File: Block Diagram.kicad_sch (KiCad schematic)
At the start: 0 parts

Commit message: Finished preliminary project schematics and architecture
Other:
- note added: "VBAT/VBUS"

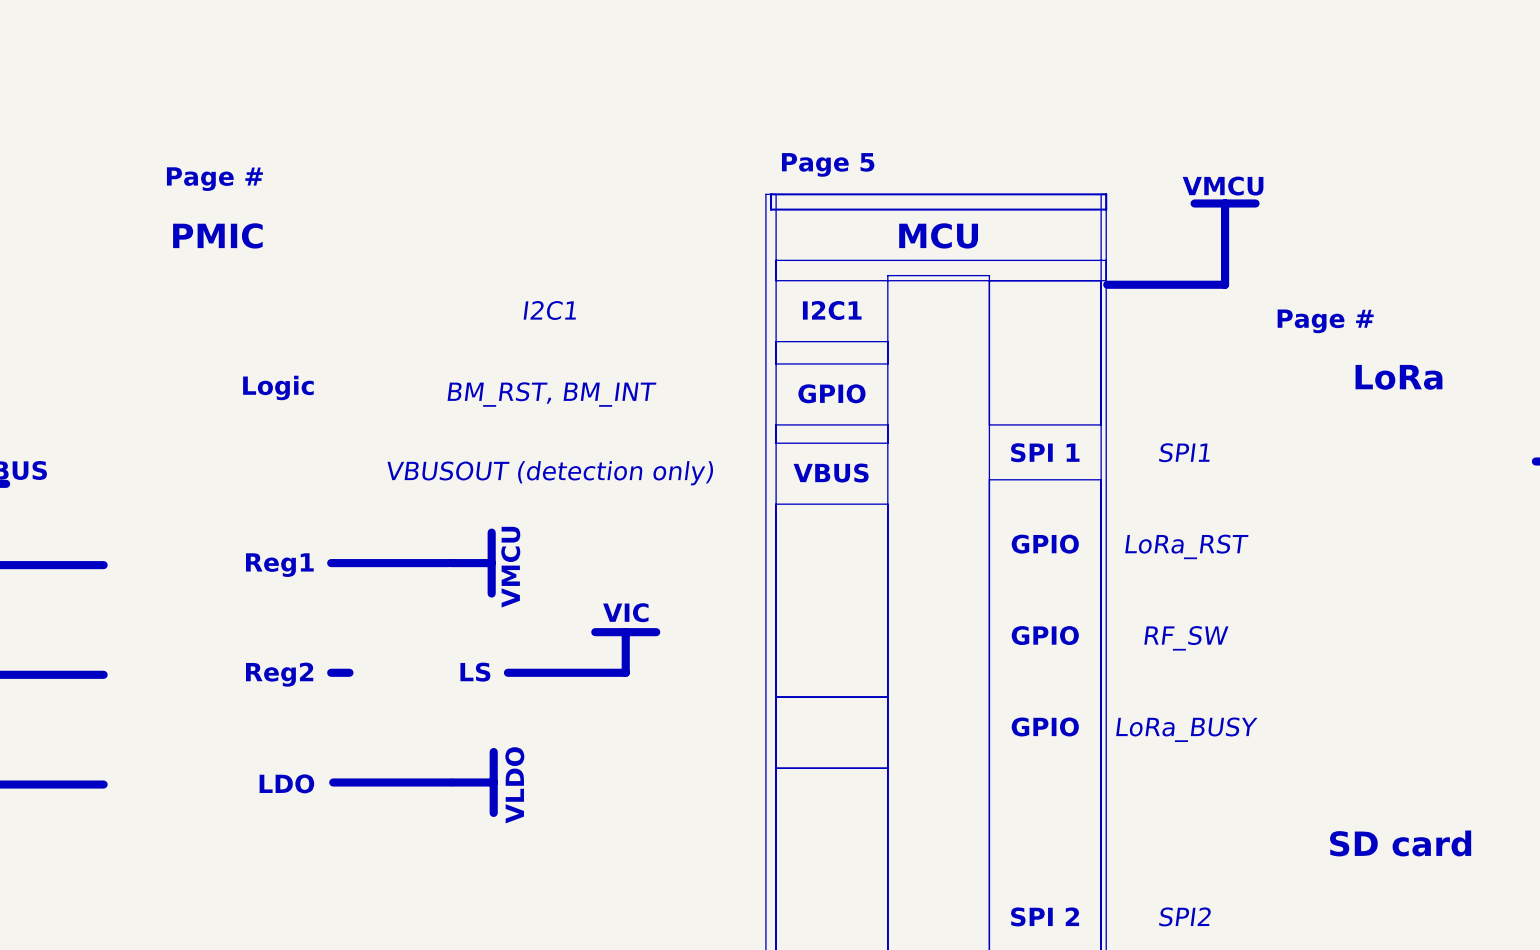
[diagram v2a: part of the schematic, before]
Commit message: Minor schematic adjustments
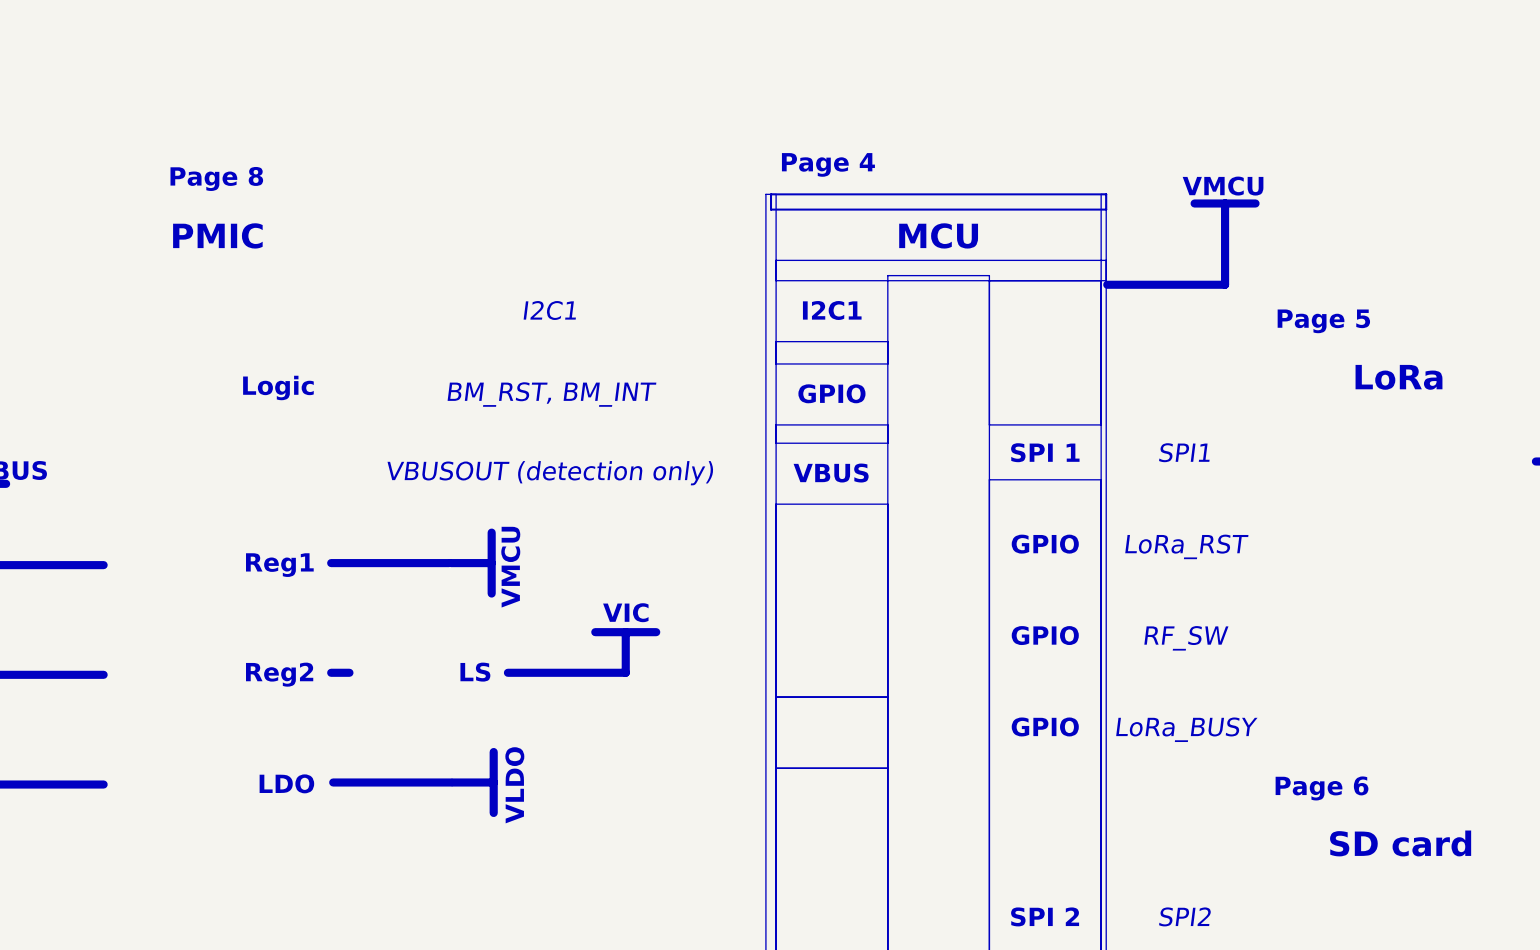
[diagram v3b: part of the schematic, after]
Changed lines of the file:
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@@
 		)
 	)
-	(text_box "Page #"
+	(text_box "Page 8"
 		(exclude_from_sim no)
 		(at 124.46 81.28 0)
-		(size 17.78 5.08)
-		(margins 1.7144 1.7144 1.7144 1.7144)
-		(stroke
-			(width -0.0001)
-			(type default)
+		(size 17.78 6.9842)
+		(margins 1.7144 1.7144 1.7144 1.7144)
+		(stroke
+			(width -0.0001)
+			(type solid)
 		)
 		(fill
@@
 			)
 			(justify right top)
+			(href "#8")
 		)
 	)
@@
 		)
 	)
+	(text_box "Page 6"
+		(exclude_from_sim no)
+		(at 264.922 157.48 0)
+		(size 17.78 6.9842)
+		(margins 1.7144 1.7144 1.7144 1.7144)
+		(stroke
+			(width -0.0001)
+			(type solid)
+		)
+		(fill
+			(type none)
+		)
+		(effects
+			(font
+				(face "Times New Roman")
+				(size 2.286 2.286)
+				(thickness 0.4572)
+				(bold yes)
+				(color 0 0 0 1)
+			)
+			(justify left top)
+			(href "#6")
+		)
+	)
 	(text_box "Target specifications:"
 		(exclude_from_sim no)
@@
 		)
 	)
+	(text_box "Page 4"
+		(exclude_from_sim no)
+		(at 203.2 79.502 0)
+		(size 24.765 6.9842)
+		(margins 1.7144 1.7144 1.7144 1.7144)
+		(stroke
+			(width -0.0001)
+			(type solid)
+		)
+		(fill
+			(type none)
+		)
+		(effects
+			(font
+				(face "Times New Roman")
+				(size 2.286 2.286)
+				(thickness 0.4572)
+				(bold yes)
+				(color 0 0 0 1)
+			)
+			(justify left top)
+			(href "#4")
+		)
+	)
 	(text_box "Page 5"
 		(exclude_from_sim no)
-		(at 203.2 79.502 0)
-		(size 24.765 5.08)
-		(margins 1.7144 1.7144 1.7144 1.7144)
-		(stroke
-			(width -0.0001)
-			(type default)
+		(at 265.176 99.06 0)
+		(size 17.78 6.9842)
+		(margins 1.7144 1.7144 1.7144 1.7144)
+		(stroke
+			(width -0.0001)
+			(type solid)
 		)
 		(fill
@@
 		)
 	)
-	(text_box "Page #"
-		(exclude_from_sim no)
-		(at 265.176 99.06 0)
-		(size 17.78 5.08)
-		(margins 1.7144 1.7144 1.7144 1.7144)
-		(stroke
-			(width -0.0001)
-			(type default)
-		)
-		(fill
-			(type none)
-		)
-		(effects
-			(font
-				(face "Times New Roman")
-				(size 2.286 2.286)
-				(thickness 0.4572)
-				(bold yes)
-				(color 0 0 0 1)
-			)
-			(justify left top)
-			(href "#8")
-		)
-	)
